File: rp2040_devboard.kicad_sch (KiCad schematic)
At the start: 25 parts, among them J1 USB_C_Receptacle_USB2.0_14P, U1 RP2040, U2 MCP1700x-330xxMB, Y1 Crystal_GND24

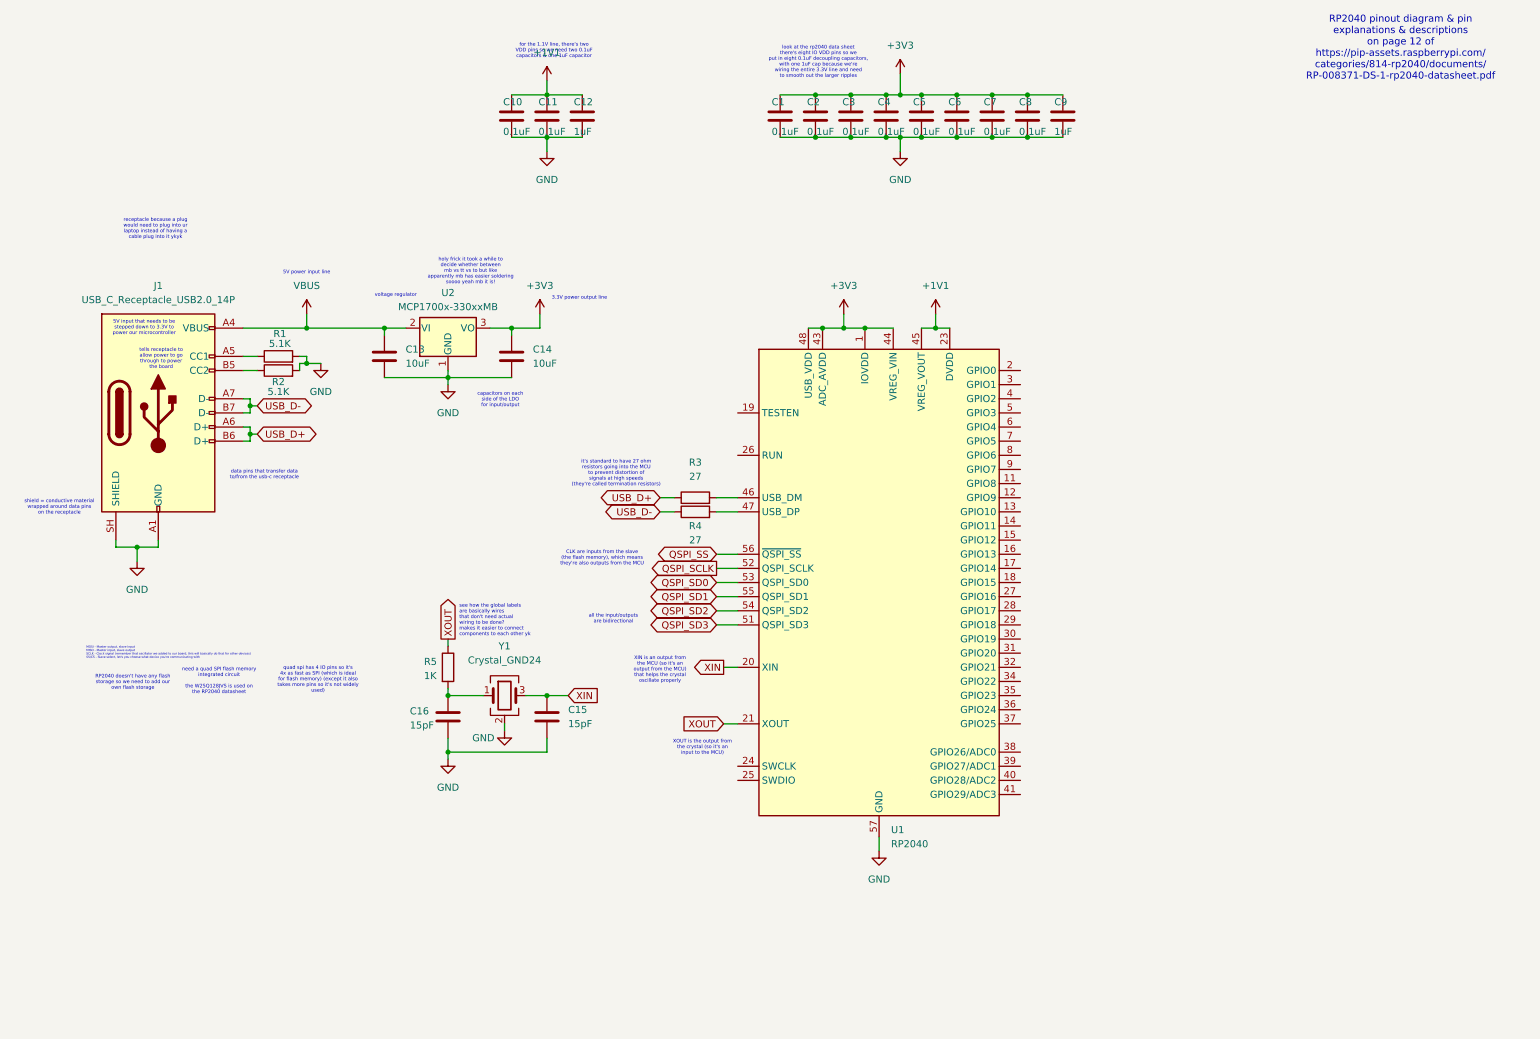
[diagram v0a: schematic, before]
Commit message: finished schematic; updated a few footprints; working on routing
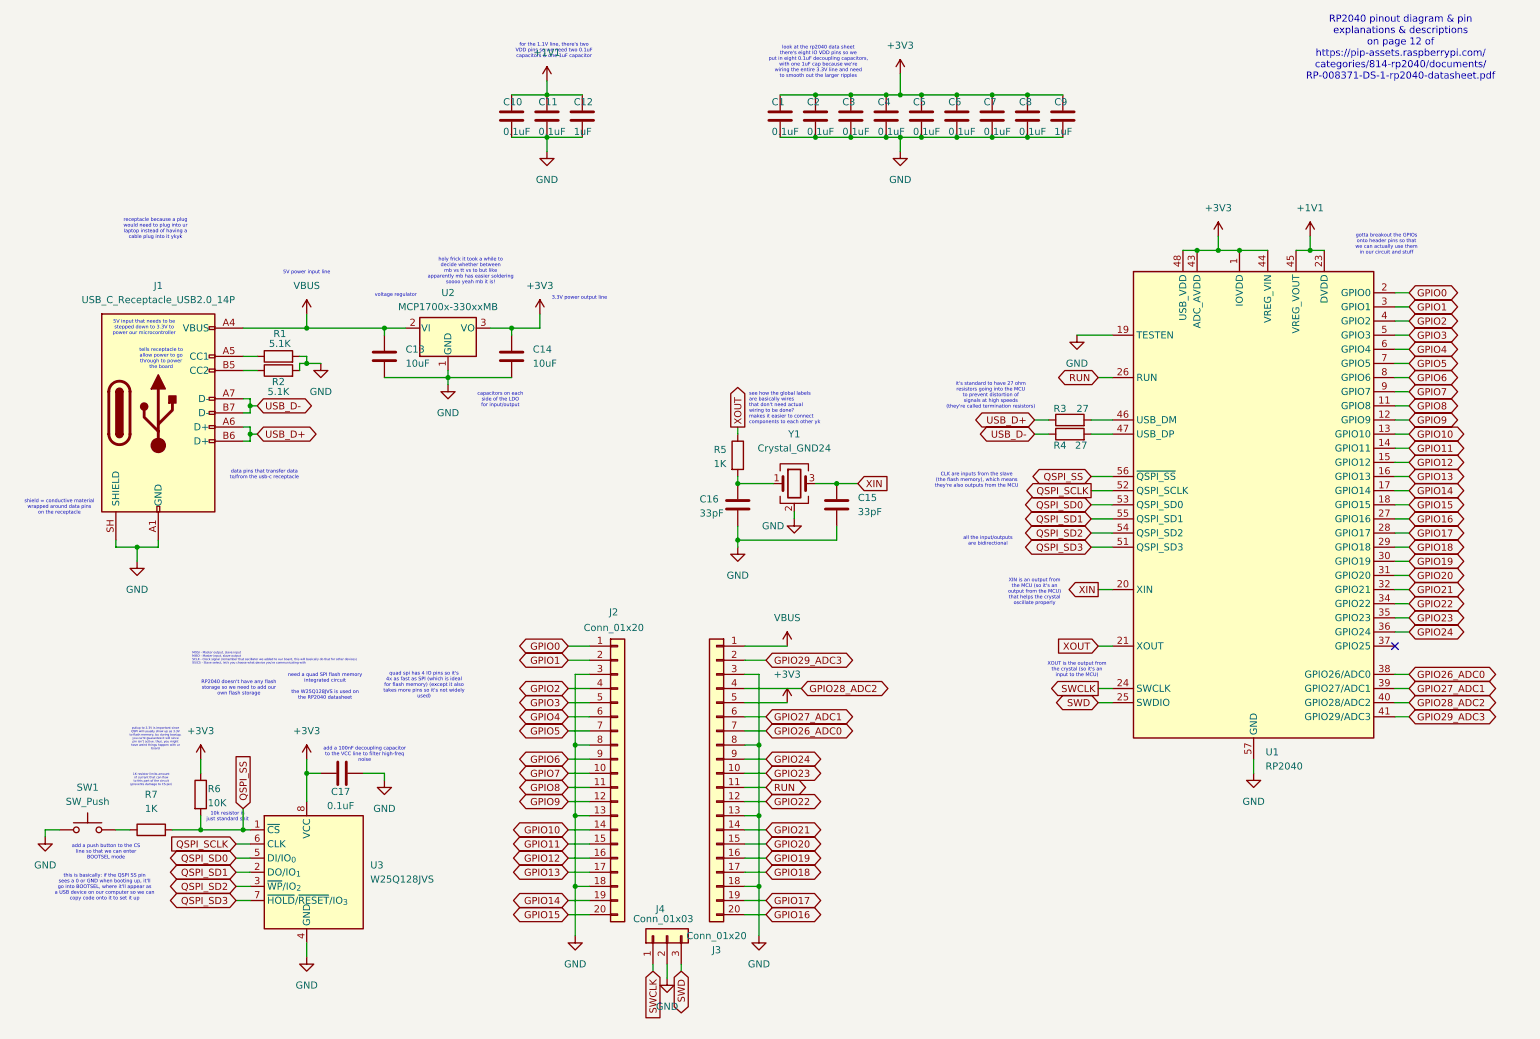
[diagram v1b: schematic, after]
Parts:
- added C17: 0.1uF, Capacitor_SMD:C_0402_1005Metric, symbol Device:C
- added J2, J3: Conn_01x20, Connector_PinHeader_2.54mm:PinHeader_1x20_P2.54mm_Vertical, symbol Connector_Generic:Conn_01x20
- added J4: Conn_01x03, Connector_PinHeader_2.54mm:PinHeader_1x03_P2.54mm_Vertical, symbol Connector_Generic:Conn_01x03
- added R6: 10K, Resistor_SMD:R_0402_1005Metric, symbol Device:R
- added R7: 1K, Resistor_SMD:R_0402_1005Metric, symbol Device:R
- added SW1: SW_Push, Button_Switch_SMD:SW_Push_SPST_NO_Alps_SKRK, symbol Switch:SW_Push
- added U3: W25Q128JVS, Package_SON:Winbond_USON-8-1EP_3x2mm_P0.5mm_EP0.2x1.6mm, symbol Memory_Flash:W25Q128JVS
- C1, C10, C11, C12, C2, C3, C4, C5, C6, C7, C8, C9: footprint (none) -> Capacitor_SMD:C_0402_1005Metric
- C13, C14: footprint (none) -> Capacitor_SMD:C_0201_0603Metric
- C15, C16: value 15pF -> 33pF; footprint (none) -> Capacitor_SMD:C_0201_0603Metric
- J1: footprint (none) -> Connector_USB:USB_C_Receptacle_HRO_TYPE-C-31-M-12
- R1, R2, R3, R4, R5: footprint (none) -> Resistor_SMD:R_0402_1005Metric
- Y1: footprint (none) -> Crystal:Crystal_SMD_3225-4Pin_3.2x2.5mm
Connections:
- net +3V3: now also C17.1, J3.5 (Pin_5), R6.1, U3.8 (VCC)
- net GND: now also U1.19 (TESTEN), C17.2, J2.13 (Pin_13), J2.18 (Pin_18), J2.3 (Pin_3), J2.8 (Pin_8), J3.13 (Pin_13), J3.18 (Pin_18), J3.3 (Pin_3), J3.8 (Pin_8), J4.2 (Pin_2), SW1.1, U3.4 (GND)
- net QSPI_SCLK: now also U3.6 (CLK)
- net QSPI_SD0: now also U3.5 (DI/IO_{0})
- net QSPI_SD1: now also U3.2 (DO/IO_{1})
- net QSPI_SD2: now also U3.3 (~{WP}/IO_{2})
- net QSPI_SD3: now also U3.7 (~{HOLD}/~{RESET}/IO_{3})
- net QSPI_SS: now also R6.2, R7.2, U3.1 (~{CS})
- net VBUS: now also J3.1 (Pin_1)
- net GPIO8: now reaches U1.11 (GPIO8)
- net GPIO8: now also J2.11 (Pin_11)
- net GPIO9: now reaches U1.12 (GPIO9)
- net GPIO9: now also J2.12 (Pin_12)
- net GPIO10: now reaches U1.13 (GPIO10)
- net GPIO10: now also J2.14 (Pin_14)
- net GPIO11: now reaches U1.14 (GPIO11)
- net GPIO11: now also J2.15 (Pin_15)
- net GPIO12: now reaches U1.15 (GPIO12)
- net GPIO12: now also J2.16 (Pin_16)
- net GPIO13: now reaches U1.16 (GPIO13)
- net GPIO13: now also J2.17 (Pin_17)
- net GPIO14: now reaches U1.17 (GPIO14)
- net GPIO14: now also J2.19 (Pin_19)
- net GPIO15: now reaches U1.18 (GPIO15)
- net GPIO15: now also J2.20 (Pin_20)
- net GPIO0: now reaches U1.2 (GPIO0)
- net GPIO0: now also J2.1 (Pin_1)
- net SWCLK: now reaches U1.24 (SWCLK)
- net SWCLK: now also J4.1 (Pin_1)
- net SWD: now reaches U1.25 (SWDIO)
- net SWD: now also J4.3 (Pin_3)
- net RUN: now reaches U1.26 (RUN)
- net RUN: now also J3.11 (Pin_11)
- net GPIO16: now reaches U1.27 (GPIO16)
- net GPIO16: now also J3.20 (Pin_20)
- net GPIO17: now reaches U1.28 (GPIO17)
- net GPIO17: now also J3.19 (Pin_19)
- net GPIO18: now reaches U1.29 (GPIO18)
- net GPIO18: now also J3.17 (Pin_17)
- net GPIO1: now reaches U1.3 (GPIO1)
- net GPIO1: now also J2.2 (Pin_2)
- net GPIO19: now reaches U1.30 (GPIO19)
- net GPIO19: now also J3.16 (Pin_16)
- net GPIO20: now reaches U1.31 (GPIO20)
- net GPIO20: now also J3.15 (Pin_15)
- net GPIO21: now reaches U1.32 (GPIO21)
- net GPIO21: now also J3.14 (Pin_14)
- net GPIO22: now reaches U1.34 (GPIO22)
- net GPIO22: now also J3.12 (Pin_12)
- net GPIO23: now reaches U1.35 (GPIO23)
- net GPIO23: now also J3.10 (Pin_10)
- net GPIO24: now reaches U1.36 (GPIO24)
- net GPIO24: now also J3.9 (Pin_9)
- net GPIO26_ADC0: now reaches U1.38 (GPIO26/ADC0)
- net GPIO26_ADC0: now also J3.7 (Pin_7)
- net GPIO27_ADC1: now reaches U1.39 (GPIO27/ADC1)
- net GPIO27_ADC1: now also J3.6 (Pin_6)
- net GPIO2: now reaches U1.4 (GPIO2)
- net GPIO2: now also J2.4 (Pin_4)
- net GPIO28_ADC2: now reaches U1.40 (GPIO28/ADC2)
- net GPIO28_ADC2: now also J3.4 (Pin_4)
- net GPIO29_ADC3: now reaches U1.41 (GPIO29/ADC3)
- net GPIO29_ADC3: now also J3.2 (Pin_2)
- net GPIO3: now reaches U1.5 (GPIO3)
- net GPIO3: now also J2.5 (Pin_5)
- net GPIO4: now reaches U1.6 (GPIO4)
- net GPIO4: now also J2.6 (Pin_6)
- net GPIO5: now reaches U1.7 (GPIO5)
- net GPIO5: now also J2.7 (Pin_7)
- net GPIO6: now reaches U1.8 (GPIO6)
- net GPIO6: now also J2.9 (Pin_9)
- net GPIO7: now reaches U1.9 (GPIO7)
- net GPIO7: now also J2.10 (Pin_10)
- new net: R7.1, SW1.2
- no-connect marks 0 -> 1
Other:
- note added: "10k resistor is just standard shit"
- note added: "1K resistor limits amount of current that can flow to this part of the circuit (prevents damage to CS pin)"
- note added: "add a 100nF decoupling capacitor to the VCC line to filter high-freq noise"
- note added: "add a push button to the CS line so that we can enter BOOTSEL mode"
- note added: "gotta breakout the GPIOs onto header pins so that we can actually use them in our circuit and stuff"
- note added: "pullup to 3.3V is important since QSPI will usually show up as 3.3V to flash memory, bu during bootup, you ca'nt guarantee it will since pin isn't active. thus, you might have weird things happen with ur board"
- note added: "this is basically: if the QSPI SS pin sees a 0 or GND when booting up, it'll go into BOOTSEL, where it'll appear as a USB device on our computer so we can copy code onto it to set it up"
- moved on the sheet: C15, C16, R3, R4, R5, U1, Y1

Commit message: fixed like 50 drc errors
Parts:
- C13, C14: footprint Capacitor_SMD:C_0201_0603Metric -> Capacitor_SMD:C_0603_1608Metric
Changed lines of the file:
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@@
 			)
 		)
-		(property "Footprint" "Capacitor_SMD:C_0201_0603Metric"
+		(property "Footprint" "Capacitor_SMD:C_0603_1608Metric"
 			(at 102.5652 81.28 0)
 			(hide yes)
@@
 			)
 		)
-		(property "Footprint" "Capacitor_SMD:C_0201_0603Metric"
+		(property "Footprint" "Capacitor_SMD:C_0603_1608Metric"
 			(at 79.7052 81.28 0)
 			(hide yes)
